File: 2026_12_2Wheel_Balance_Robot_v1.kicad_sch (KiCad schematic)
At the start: 56 parts, among them J1 Conn_01x04, J2 CONN_MPU6050, J3 USB_C_Receptacle_USB2.0_14P, J4 ESP_Conn, J5 BATT_CONN, J6 M1_CONN, J7 M2_CONN, J8 ENCODER_CONN, J9 MT6701_CONN, SW2 SW_uP_Reset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

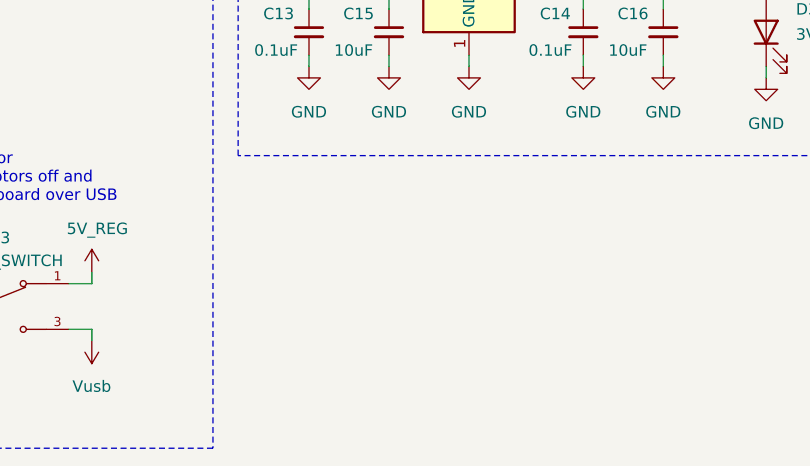
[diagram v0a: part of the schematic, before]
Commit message: Updated Gerbers to include mounting holes
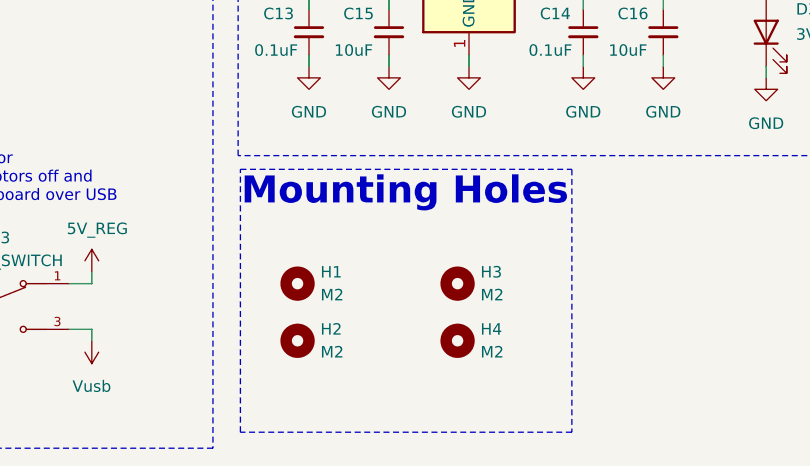
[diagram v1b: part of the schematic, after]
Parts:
- added H1, H2, H3, H4: M2, MountingHole:MountingHole_2.2mm_M2, symbol Mechanical:MountingHole
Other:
- note added: "Mounting Holes"
